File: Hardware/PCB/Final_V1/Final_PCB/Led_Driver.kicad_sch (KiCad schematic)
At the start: 15 parts, among them IC2 PCA9955BTWJ

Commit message: fixed Schematics
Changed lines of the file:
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@@
 	(wire
 		(pts
-			(xy 148.59 132.08) (xy 148.59 134.62)
+			(xy 148.59 132.08) (xy 148.59 133.35)
 		)
 		(stroke
@@
 	(symbol
 		(lib_id "power:GND")
-		(at 148.59 134.62 0)
+		(at 148.59 133.35 0)
 		(unit 1)
 		(exclude_from_sim no)
@@
 		(fields_autoplaced yes)
 		(property "Reference" "#PWR035"
-			(at 148.59 140.97 0)
+			(at 148.59 139.7 0)
 			(effects
 				(font
@@
 		)
 		(property "Value" "GND"
-			(at 148.59 139.7 0)
+			(at 148.59 138.43 0)
 			(effects
 				(font
@@
 		)
 		(property "Footprint" ""
-			(at 148.59 134.62 0)
+			(at 148.59 133.35 0)
 			(effects
 				(font
@@
 		)
 		(property "Datasheet" ""
-			(at 148.59 134.62 0)
+			(at 148.59 133.35 0)
 			(effects
 				(font
@@
 		)
 		(property "Description" "Power symbol creates a global label with name \"GND\" , ground"
-			(at 148.59 134.62 0)
-			(effects
-				(font
+			(at 148.59 133.35 0)
+			(effects
+				(font

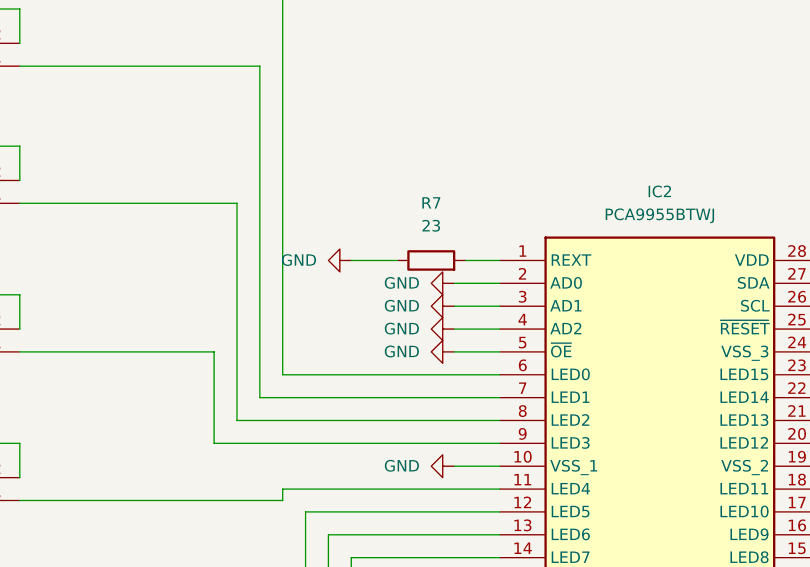
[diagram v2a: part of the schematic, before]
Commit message: fixed curcuit, mainly the charge curcuit
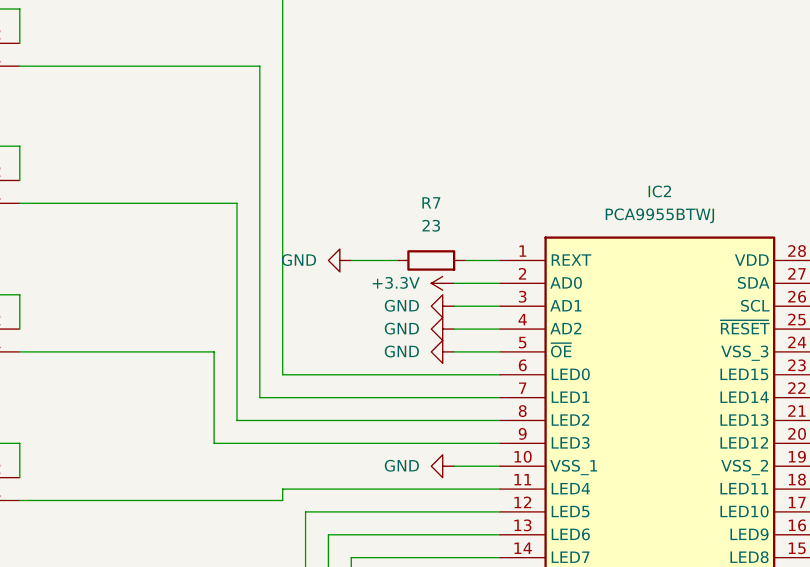
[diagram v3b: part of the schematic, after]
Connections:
- net +3.3V: now also IC2.2 (AD0)
- net GND: no longer IC2.2 (AD0)
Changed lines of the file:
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@@
+	(symbol
+		(lib_id "power:+3.3V")
+		(at 125.73 86.36 90)
+		(unit 1)
+		(exclude_from_sim no)
+		(in_bom yes)
+		(on_board yes)
+		(dnp no)
+		(fields_autoplaced yes)
+		(property "Reference" "#PWR050"
+			(at 129.54 86.36 0)
+			(effects
+				(font
+					(size 1.27 1.27)
+				)
+				(hide yes)
+			)
+		)
+		(property "Value" "+3.3V"
+			(at 121.92 86.3599 90)
+			(effects
+				(font
+					(size 1.27 1.27)
+				)
+				(justify left)
+			)
+		)
+		(property "Footprint" ""
+			(at 125.73 86.36 0)
+			(effects
+				(font
+					(size 1.27 1.27)
+				)
+				(hide yes)
+			)
+		)
+		(property "Datasheet" ""
+			(at 125.73 86.36 0)
+			(effects
+				(font
+					(size 1.27 1.27)
+				)
+				(hide yes)
+			)
+		)
+		(property "Description" "Power symbol creates a global label with name \"+3.3V\""
+			(at 125.73 86.36 0)
+			(effects
+				(font
+					(size 1.27 1.27)
+				)
+				(hide yes)
+			)
+		)
+		(pin "1"
+		)
+		(instances
+			(project "Final_PCB"
+				(path "/3cedac76-cdf6-4427-9720-a412bd9af7e2/31097afd-7b19-4340-a34a-5b2b647d4078"
+					(reference "#PWR050")
+					(unit 1)
+				)
+			)
+		)
+	)
 	(symbol
 		(lib_id "power:+3.3V")
@@
 					(unit 1)
 				)
-			)
-		)
-	)
-	(symbol
-		(lib_id "power:GND")
-		(at 125.73 86.36 270)
-		(unit 1)
-		(exclude_from_sim no)
-		(in_bom yes)
-		(on_board yes)
-		(dnp no)
-		(fields_autoplaced yes)
-		(property "Reference" "#PWR030"
-			(at 119.38 86.36 0)
-			(effects
-				(font
-					(size 1.27 1.27)
-				)
-				(hide yes)
-			)
-		)
-		(property "Value" "GND"
-			(at 121.92 86.3599 90)
-			(effects
-				(font
-					(size 1.27 1.27)
-				)
-				(justify right)
-			)
-		)
-		(property "Footprint" ""
-			(at 125.73 86.36 0)
-			(effects
-				(font
-					(size 1.27 1.27)
-				)
-				(hide yes)
-			)
-		)
-		(property "Datasheet" ""
-			(at 125.73 86.36 0)
-			(effects
-				(font
-					(size 1.27 1.27)
-				)
-				(hide yes)
-			)
-		)
-		(property "Description" "Power symbol creates a global label with name \"GND\" , ground"
-			(at 125.73 86.36 0)
-			(effects
-				(font
-					(size 1.27 1.27)
-				)
-				(hide yes)
-			)
-		)
-		(pin "1"
-		)
-		(instances
-			(project "Final_PCB"
-				(path "/3cedac76-cdf6-4427-9720-a412bd9af7e2/31097afd-7b19-4340-a34a-5b2b647d4078"
-					(reference "#PWR030")
-					(unit 1)
-				)

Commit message: #1: Add footprints to the components
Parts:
- IC2: footprint SOP65P640X110-29N -> custom:SOP65P640X110-29N
- LED10, LED11, LED12, LED9: footprint LSE65FBBDA11 -> custom:LSE65FBBDA11
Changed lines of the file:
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@@
 			)
 		)
-		(property "Footprint" "LSE65FBBDA11"
+		(property "Footprint" "custom:LSE65FBBDA11"
 			(at 208.28 197.79 0)
 			(effects
@@
 			)
 		)
-		(property "Footprint" "LSE65FBBDA11"
+		(property "Footprint" "custom:LSE65FBBDA11"
 			(at 207.01 247.32 0)
 			(effects
@@
 			)
 		)
-		(property "Footprint" "SOP65P640X110-29N"
+		(property "Footprint" "custom:SOP65P640X110-29N"
 			(at 162.56 178.74 0)
 			(effects
@@
 			)
 		)
-		(property "Footprint" "LSE65FBBDA11"
+		(property "Footprint" "custom:LSE65FBBDA11"
 			(at 207.01 229.54 0)
 			(effects
@@
 			)
 		)
-		(property "Footprint" "LSE65FBBDA11"
+		(property "Footprint" "custom:LSE65FBBDA11"
 			(at 208.28 213.03 0)
 			(effects

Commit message: started layouting
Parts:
- removed LED11, LED12: LS_E65F-BBDA-1-1, custom:LSE65FBBDA11, symbol LS_E65F-BBDA-1-1:LS_E65F-BBDA-1-1
- LED1, LED2, LED3, LED4, LED5, LED6, LED7, LED8: footprint LS_E65F-BBDA-1-1:LSE65FBBDA11 -> custom:LSE65FBBDA11
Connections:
- no-connect marks 4 -> 6
